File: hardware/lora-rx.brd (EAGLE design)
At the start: 46.4 x 17.8 mm, 32 parts, among them J1 USB-A-H, J2 SMA_EDGE, J3 DNP, U1 STM32L052K8, U2 SX1278, U3 TPS70933

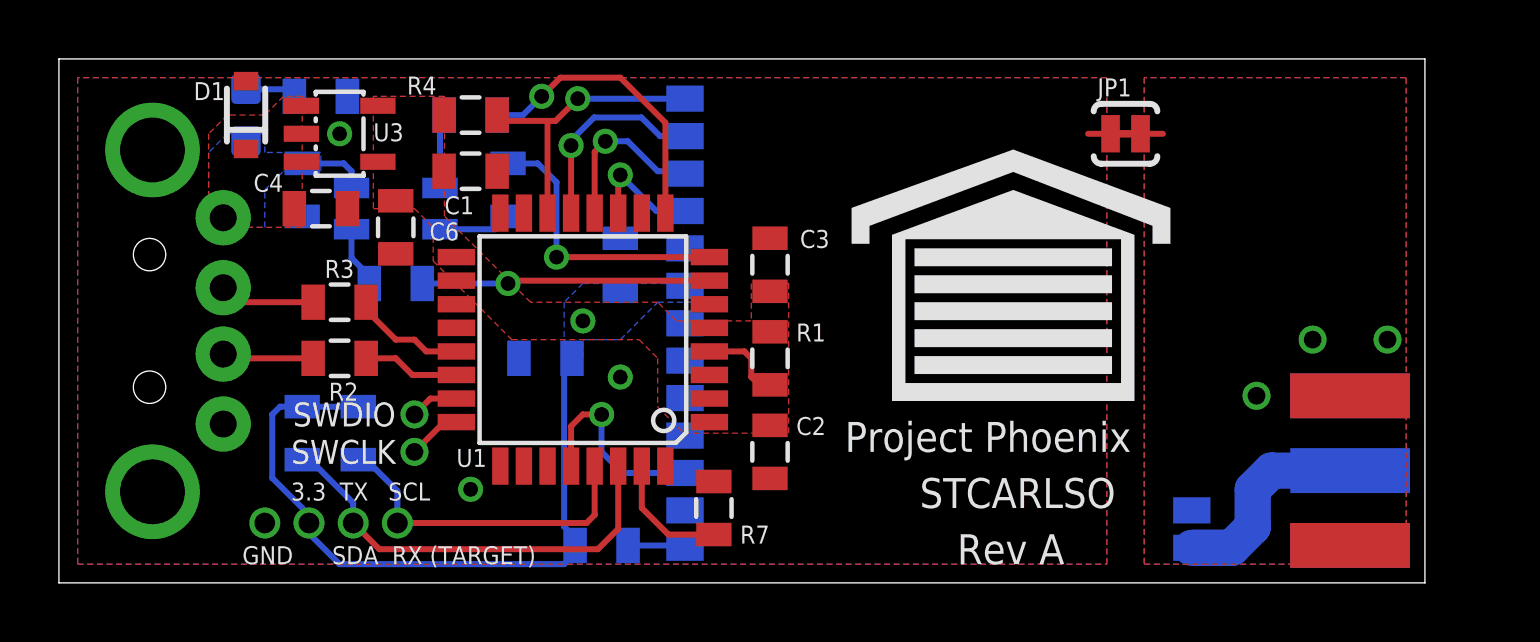
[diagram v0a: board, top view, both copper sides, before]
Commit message: Initial route for HAB v3 modular base board
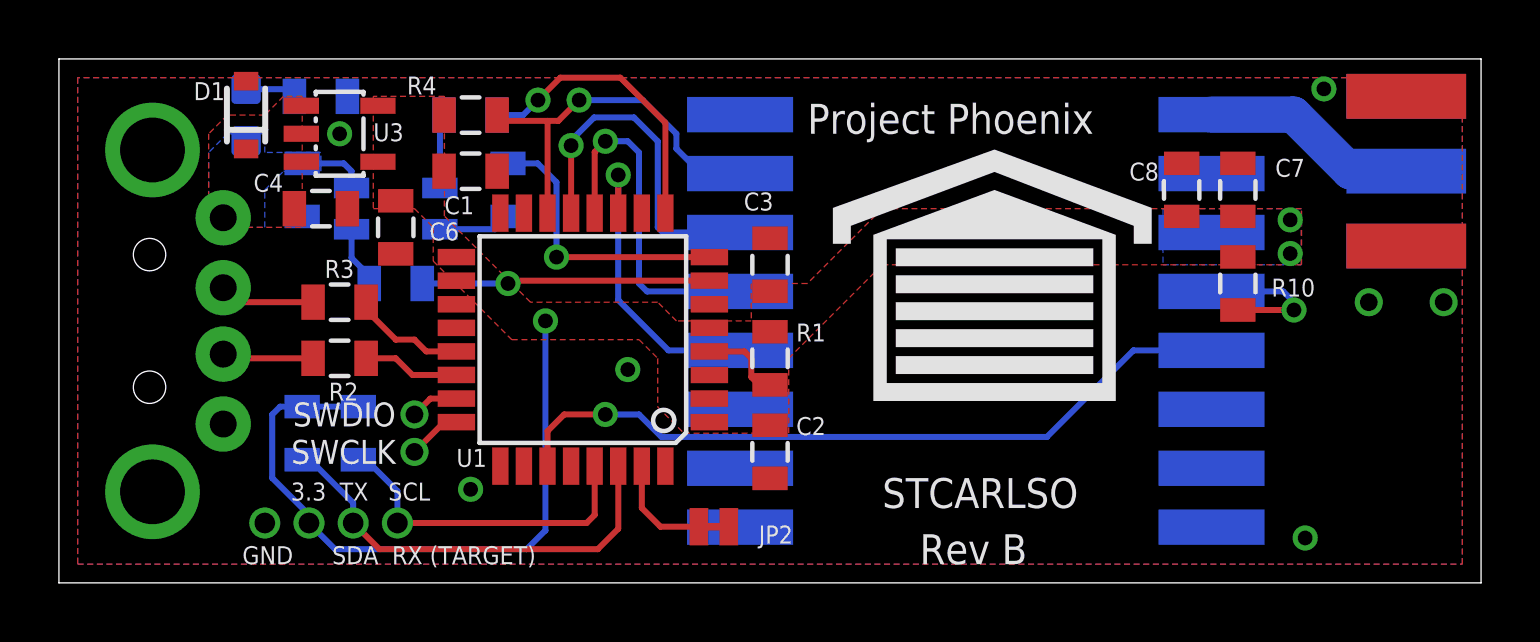
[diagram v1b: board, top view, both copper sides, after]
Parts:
- removed JP1: GND, SparkFun-Passives:PAD-JUMPER-2-NC_BY_TRACE_YES_SILK
- removed R7: 10K, SparkFun-Passives:0805
- added JP2: (no value), SparkFun-Jumpers:SMT-JUMPER_2_NC_TRACE_NO-SILK
- U2: value SX1278 -> RA01; device HAB:DRF1278F -> HAB:RA01
- moved C7 24.2 mm to (40.0, 13.3), flipped to the top, turned to 90 degrees
- moved R10 23.3 mm to (40.0, 10.2), flipped to the top, turned to 90 degrees
- moved C8 19.2 mm to (38.1, 13.3), flipped to the top
- moved J2 10.3 mm to (45.7, 11.4)
- moved U2 1.27 mm to (31.1, 8.89), turned to 0 degrees
- moved U$1 0.63 mm to (31.8, 9.53)
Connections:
- removed net AGND: J2.GND@0, J2.GND@1, J2.GND@2, J2.GND@3, JP1.2, U2.14
- net !SS!: now also U2.15; no longer U2.13
- net !SX_RST!: now also U2.4; no longer U2.1
- net 3.3V: now also U2.3; no longer U2.8
- net ANT: now also U2.1; no longer U2.15
- net BOOT0: now also JP2.2; no longer R7.2
- net GND: now also J2.GND@0, J2.GND@1, J2.GND@2, J2.GND@3, JP2.1, U2.16, U2.2; no longer JP1.1, R7.1
- net INT: now also U1.27, U2.5; no longer U1.28, U2.3
- net MISO: now also U2.13; no longer U2.11
- net MOSI: now also U2.14; no longer U2.12
- net SCK: now also U2.12; no longer U2.10
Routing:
- net INT: track 6.95 -> 25.5 mm
- net SCK: track 4.03 -> 10.4 mm
- net MISO: track 5.75 -> 11.9 mm
- net MOSI: track 6.92 -> 11.9 mm
- net !SS!: track 9.90 -> 13.1 mm
- net !SX_RST!: track 1.96 -> 5.12 mm, vias 0 -> 1
- net 3.3V: track 24.1 -> 23.0 mm, vias 1 -> 3
- net GND: track 0.76 -> 0.00 mm, vias 3 -> 7
- net AGND: track 0.76 -> 0.00 mm, vias 3 -> 0
- net BOOT0: track 4.24 -> 3.62 mm
- removed copper zone on layer 1, net AGND
- removed copper zone on layer 16, net AGND
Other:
- board size 46.4 x 17.8 mm -> 48.3 x 17.8 mm
- board text added: "Rev B"
- board text removed: "Rev A"
